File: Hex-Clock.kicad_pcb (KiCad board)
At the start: 2 copper layers, 77.1 x 89 mm, 20 parts

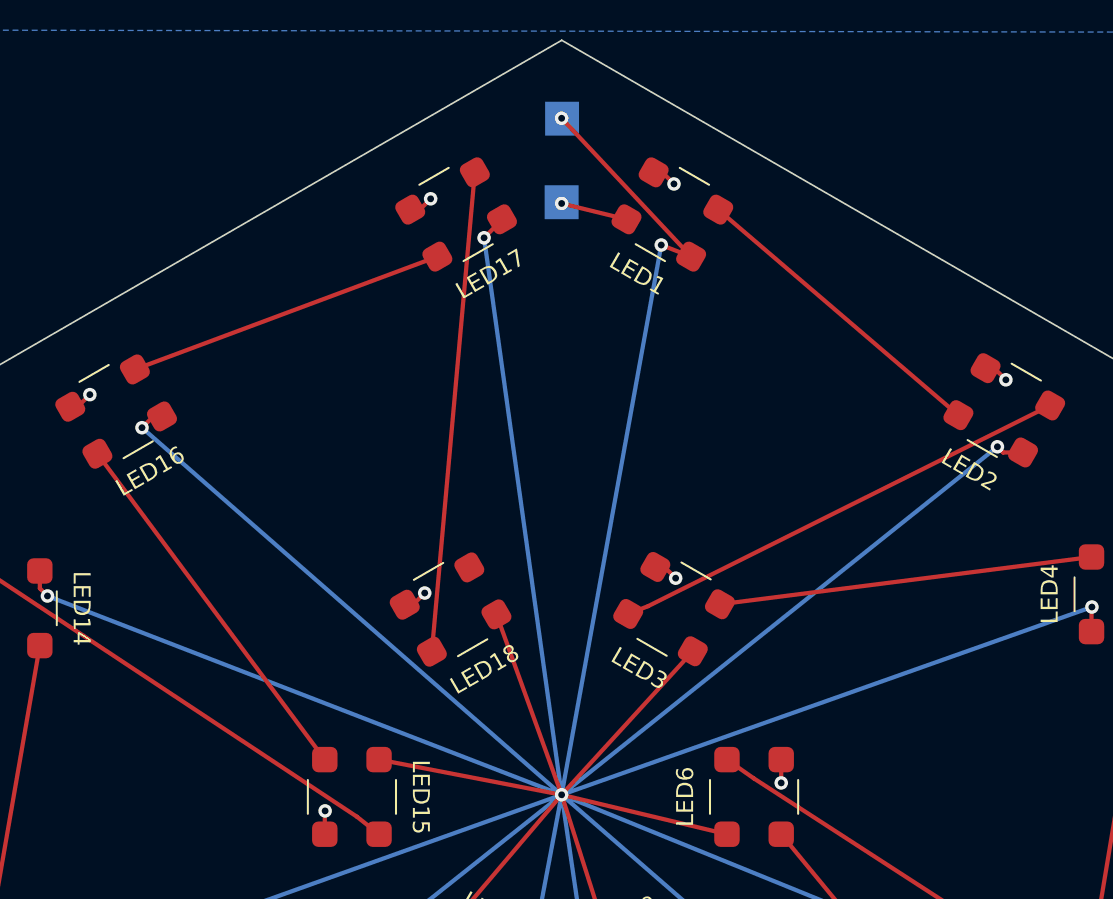
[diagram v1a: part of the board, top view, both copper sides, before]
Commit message: Added ground pad
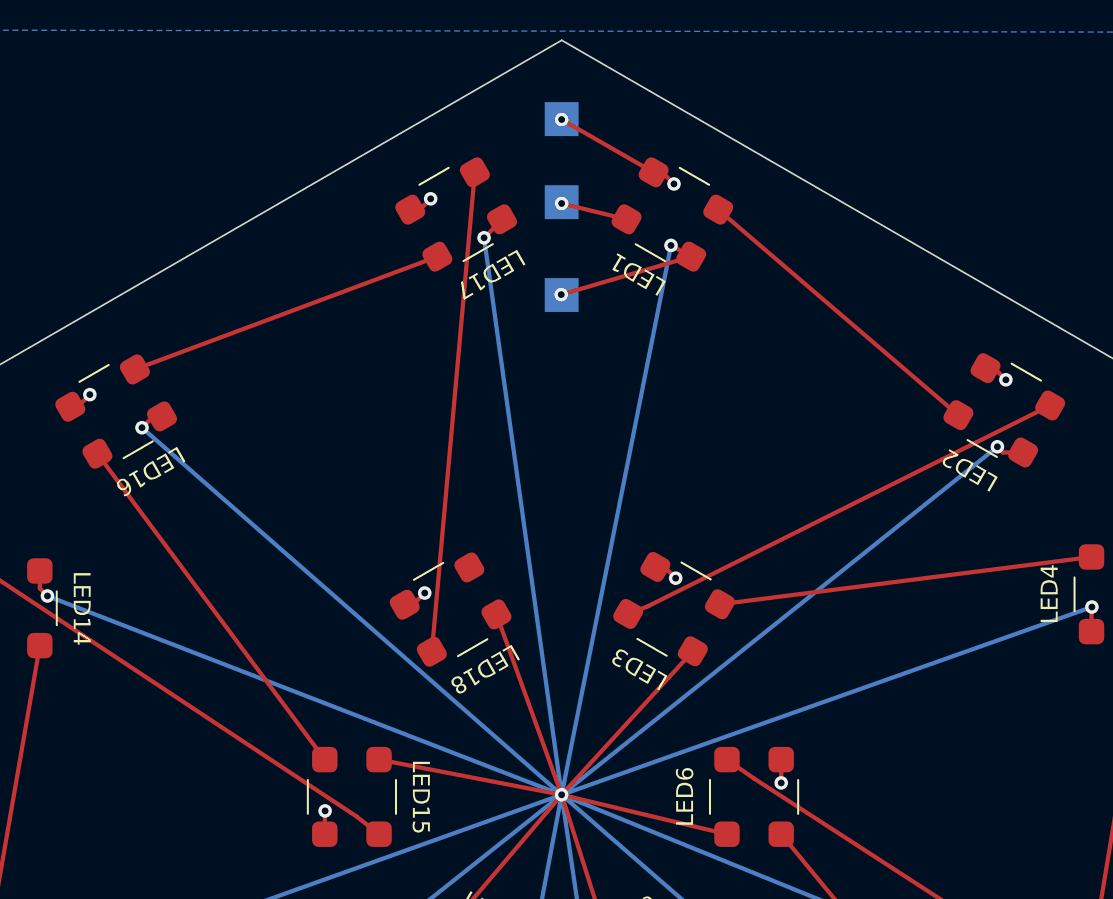
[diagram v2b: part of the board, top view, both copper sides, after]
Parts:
- added GND: TestPoint_Pad_2.0x2.0mm, TestPoint:TestPoint_Pad_2.0x2.0mm, B.Cu at (150.2, 61.3)
- moved +5V 10.4 mm to (150.2, 71.7)
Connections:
- +5V pad 1: (no net) -> +5V
- DATA IN pad 1: (no net) -> Data IN
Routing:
- net GND: track 26.0 -> 32.2 mm, vias 18 -> 19
- net +5V: track 491.8 -> 488.1 mm
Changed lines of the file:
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@@
     (property "Sheetname" "")
     (attr smd)
-    (fp_text reference "LED18" (at 0.01 -4.06 -330 unlocked) (layer "F.SilkS")
+    (fp_text reference "LED18" (at 0.01 -4.06 -150 unlocked) (layer "F.SilkS")
       (effects (font (size 1 1) (thickness 0.15)))
     )
@@
     (property "Sheetname" "")
     (attr smd)
-    (fp_text reference "LED1" (at 0.01 -4.06 -30 unlocked) (layer "F.SilkS")
+    (fp_text reference "LED1" (at 0.01 -4.06 150 unlocked) (layer "F.SilkS")
       (effects (font (size 1 1) (thickness 0.15)))
     )
@@
     (property "Sheetname" "")
     (attr smd)
-    (fp_text reference "LED2" (at 0.01 -4.06 330 unlocked) (layer "F.SilkS")
+    (fp_text reference "LED2" (at 0.01 -4.06 150 unlocked) (layer "F.SilkS")
       (effects (font (size 1 1) (thickness 0.15)))
     )
@@
     (property "Sheetname" "")
     (attr smd)
-    (fp_text reference "LED16" (at 0.01 -4.06 30 unlocked) (layer "F.SilkS")
+    (fp_text reference "LED16" (at 0.01 -4.06 -150 unlocked) (layer "F.SilkS")
       (effects (font (size 1 1) (thickness 0.15)))
     )
@@
     (property "Sheetname" "")
     (attr smd)
-    (fp_text reference "LED17" (at 0.01 -4.06 -330 unlocked) (layer "F.SilkS")
+    (fp_text reference "LED17" (at 0.01 -4.06 -150 unlocked) (layer "F.SilkS")
       (effects (font (size 1 1) (thickness 0.15)))
     )
@@
     (property "Sheetname" "")
     (attr smd)
-    (fp_text reference "LED3" (at 0.01 -4.06 330 unlocked) (layer "F.SilkS")
+    (fp_text reference "LED3" (at 0.01 -4.06 150 unlocked) (layer "F.SilkS")
       (effects (font (size 1 1) (thickness 0.15)))
     )
@@
   )
   (footprint "TestPoint:TestPoint_Pad_2.0x2.0mm" (layer "B.Cu")
-    (at 150.2 61.275 180)
+    (at 150.175 71.675 180)
     (descr "SMD rectangular pad as test Point, square 2.0mm side length")
     (tags "test point SMD pad rectangle square")
@@
     (fp_line (start 1.5 -1.5) (end -1.5 -1.5) (layer "B.CrtYd") (width 0.05))
     (fp_line (start -1.5 1.5) (end 1.5 1.5) (layer "B.CrtYd") (width 0.05))
-    (pad "1" smd rect (at 0 0 180) (size 2 2) (layers "B.Cu" "B.Mask"))
+    (pad "1" smd rect (at 0 0 180) (size 2 2) (layers "B.Cu" "B.Mask")
+      (net 1 "+5V"))
   )
   (footprint "TestPoint:TestPoint_Pad_2.0x2.0mm" (layer "B.Cu")
@@
       (effects (font (size 1 1) (thickness 0.15)) (justify mirror))
     )
+    (fp_line (start 1.2 -1.2) (end -1.2 -1.2) (layer "B.SilkS") (width 0.12))
+    (fp_line (start -1.2 1.2) (end 1.2 1.2) (layer "B.SilkS") (width 0.12))
+    (fp_line (start -1.2 -1.2) (end -1.2 1.2) (layer "B.SilkS") (width 0.12))
     (fp_line (start 1.2 1.2) (end 1.2 -1.2) (layer "B.SilkS") (width 0.12))
+    (fp_line (start -1.5 1.5) (end 1.5 1.5) (layer "B.CrtYd") (width 0.05))
+    (fp_line (start 1.5 -1.5) (end -1.5 -1.5) (layer "B.CrtYd") (width 0.05))
+    (fp_line (start 1.5 -1.5) (end 1.5 1.5) (layer "B.CrtYd") (width 0.05))
+    (fp_line (start -1.5 1.5) (end -1.5 -1.5) (layer "B.CrtYd") (width 0.05))
+    (pad "1" smd rect (at 0 0 180) (size 2 2) (layers "B.Cu" "B.Mask")
+      (net 4 "Data IN"))
+  )
+  (footprint "TestPoint:TestPoint_Pad_2.0x2.0mm" (layer "B.Cu")
+    (at 150.175 61.3 180)
+    (descr "SMD rectangular pad as test Point, square 2.0mm side length")
+    (tags "test point SMD pad rectangle square")
+    (attr exclude_from_pos_files exclude_from_bom)
+    (fp_text reference "GND" (at 0 1.998) (layer "B.SilkS")
+      (effects (font (size 1 1) (thickness 0.15)) (justify mirror))
+    )
+    (fp_text value "TestPoint_Pad_2.0x2.0mm" (at 0 -2.05) (layer "B.Fab") hide
+      (effects (font (size 1 1) (thickness 0.15)) (justify mirror))
+    )
+    (fp_text user "${REFERENCE}" (at 0 2) (layer "B.Fab") hide
+      (effects (font (size 1 1) (thickness 0.15)) (justify mirror))
+    )
     (fp_line (start 1.2 -1.2) (end -1.2 -1.2) (layer "B.SilkS") (width 0.12))
+    (fp_line (start -1.2 1.2) (end 1.2 1.2) (layer "B.SilkS") (width 0.12))
     (fp_line (start -1.2 -1.2) (end -1.2 1.2) (layer "B.SilkS") (width 0.12))
-    (fp_line (start -1.2 1.2) (end 1.2 1.2) (layer "B.SilkS") (width 0.12))
+    (fp_line (start 1.2 1.2) (end 1.2 -1.2) (layer "B.SilkS") (width 0.12))
+    (fp_line (start -1.5 1.5) (end 1.5 1.5) (layer "B.CrtYd") (width 0.05))
+    (fp_line (start 1.5 -1.5) (end -1.5 -1.5) (layer "B.CrtYd") (width 0.05))
+    (fp_line (start 1.5 -1.5) (end 1.5 1.5) (layer "B.CrtYd") (width 0.05))
     (fp_line (start -1.5 1.5) (end -1.5 -1.5) (layer "B.CrtYd") (width 0.05))
-    (fp_line (start 1.5 -1.5) (end 1.5 1.5) (layer "B.CrtYd") (width 0.05))
-    (fp_line (start 1.5 -1.5) (end -1.5 -1.5) (layer "B.CrtYd") (width 0.05))
-    (fp_line (start -1.5 1.5) (end 1.5 1.5) (layer "B.CrtYd") (width 0.05))
-    (pad "1" smd rect (at 0 0 180) (size 2 2) (layers "B.Cu" "B.Mask"))
+    (pad "1" smd rect (at 0 0 180) (size 2 2) (layers "B.Cu" "B.Mask")
+      (net 3 "GND"))
   )
   (gr_line (start 188.719065 78.9) (end 150.180935 101.15) (layer "Dwgs.User") (width 0.1))
@@
   (gr_line (start 150.180935 145.65) (end 188.719066 123.4) (layer "Edge.Cuts") (width 0.1))
   (segment (start 143.489359 132.614359) (end 144.125 133.25) (width 0.25) (layer "F.Cu") (net 1))
+  (segment (start 157.811191 69.410641) (end 156.625 68.75) (width 0.25) (layer "F.Cu") (net 1))
   (segment (start 181.425 114.064031) (end 181.425 115.15) (width 0.25) (layer "F.Cu") (net 1))
-  (segment (start 157.811191 69.410641) (end 156.05 68.725) (width 0.25) (layer "F.Cu") (net 1))
   (segment (start 146.655256 67.244744) (end 145.6 68.3) (width 0.25) (layer "F.Cu") (net 1))
   (segment (start 177.386191 80.960641) (end 176.210641 80.960641) (width 0.25) (layer "F.Cu") (net 1))
@@
   (segment (start 159.925 103.475) (end 150.175 101.15) (width 0.25) (layer "F.Cu") (net 1))
   (segment (start 146.655256 67.210641) (end 146.655256 67.244744) (width 0.25) (layer "F.Cu") (net 1))
-  (segment (start 157.811191 69.410641) (end 150.175 61.25) (width 0.25) (layer "F.Cu") (net 1))
   (segment (start 119.4 88.975) (end 119.85 89.425) (width 0.25) (layer "F.Cu") (net 1))
   (segment (start 139.405935 99.075) (end 150.175 101.15) (width 0.25) (layer "F.Cu") (net 1))
+  (segment (start 157.811191 69.410641) (end 150.15 71.65) (width 0.25) (layer "F.Cu") (net 1))
   (segment (start 174.094744 123.639359) (end 174.610641 123.639359) (width 0.25) (layer "F.Cu") (net 1))
   (segment (start 124.002495 121.929097) (end 123.512757 121.439359) (width 0.25) (layer "F.Cu") (net 1))
@@
   (via (at 119.85 89.425) (size 0.8) (drill 0.4) (layers "F.Cu" "B.Cu") (free) (net 1))
   (via (at 181.45 90.075) (size 0.8) (drill 0.4) (layers "F.Cu" "B.Cu") (free) (net 1))
-  (via (at 150.175 61.25) (size 0.8) (drill 0.4) (layers "F.Cu" "B.Cu") (free) (net 1))
+  (via (at 150.15 71.65) (size 0.8) (drill 0.4) (layers "F.Cu" "B.Cu") (free) (net 1))
   (via (at 144.125 133.25) (size 0.8) (drill 0.4) (layers "F.Cu" "B.Cu") (free) (net 1))
   (via (at 150.175 101.15) (size 0.8) (drill 0.4) (layers "F.Cu" "B.Cu") (free) (net 1))
   (via (at 125.425 79.5) (size 0.8) (drill 0.4) (layers "F.Cu" "B.Cu") (free) (net 1))
-  (via (at 156.05 68.725) (size 0.8) (drill 0.4) (layers "F.Cu" "B.Cu") (free) (net 1))
+  (via (at 156.625 68.75) (size 0.8) (drill 0.4) (layers "F.Cu" "B.Cu") (free) (net 1))
   (via (at 145.6 68.3) (size 0.8) (drill 0.4) (layers "F.Cu" "B.Cu") (free) (net 1))
   (via (at 175.275 122.975) (size 0.8) (drill 0.4) (layers "F.Cu" "B.Cu") (free) (net 1))
   (via (at 154.95 133.725) (size 0.8) (drill 0.4) (layers "F.Cu" "B.Cu") (free) (net 1))
   (via (at 119.4 112.15) (size 0.8) (drill 0.4) (layers "F.Cu" "B.Cu") (free) (net 1))
+  (segment (start 156.625 68.75) (end 150.175 101.15) (width 0.25) (layer "B.Cu") (net 1))
   (segment (start 119.4 112.15) (end 150.175 101.15) (width 0.25) (layer "B.Cu") (net 1))
   (segment (start 125.425 79.5) (end 150.175 101.15) (width 0.25) (layer "B.Cu") (net 1))
@@
   (segment (start 124.002495 121.929097) (end 150.175 101.15) (width 0.25) (layer "B.Cu") (net 1))
   (segment (start 175.875 80.625) (end 150.175 101.15) (width 0.25) (layer "B.Cu") (net 1))
-  (segment (start 156.05 68.725) (end 150.175 101.15) (width 0.25) (layer "B.Cu") (net 1))
   (segment (start 181.075702 113.714733) (end 150.175 101.15) (width 0.25) (layer "B.Cu") (net 1))
   (segment (start 175.275 122.975) (end 150.175 101.15) (width 0.25) (layer "B.Cu") (net 1))
@@
   (segment (start 159.280256 135.385641) (end 158.814359 135.385641) (width 0.25) (layer "F.Cu") (net 3))
   (segment (start 141.410641 89.939359) (end 142.1 89.25) (width 0.25) (layer "F.Cu") (net 3))
+  (segment (start 155.600679 64.439359) (end 150.175 61.325) (width 0.25) (layer "F.Cu") (net 3))
   (segment (start 184.625 87.125) (end 184.625 88.45) (width 0.25) (layer "F.Cu") (net 3))
   (segment (start 184.625 112.1) (end 184.6 112.125) (width 0.25) (layer "F.Cu") (net 3))
@@
   (via (at 116.2 90.975) (size 0.8) (drill 0.4) (layers "F.Cu" "B.Cu") (free) (net 3))
   (via (at 142.1 89.25) (size 0.8) (drill 0.4) (layers "F.Cu" "B.Cu") (free) (net 3))
+  (via (at 150.175 61.325) (size 0.8) (drill 0.4) (layers "F.Cu" "B.Cu") (free) (net 3))
   (segment (start 154.000679 67.210641) (end 150.175 66.275) (width 0.25) (layer "F.Cu") (net 4))
   (via (at 150.175 66.275) (size 0.8) (drill 0.4) (layers "F.Cu" "B.Cu") (free) (net 4))
